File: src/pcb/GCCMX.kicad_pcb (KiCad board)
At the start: 2 copper layers, 341.2 x 155.5 mm, 45 parts, among them J1 Inputs Female, J2 Debug In, J3 Debug Out, J6 USB-IN, J7 USB-OUT, J8 Brook Out

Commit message: pushing everything up from prior work
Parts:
- removed the G*** at (82.0, 207.7) (x2)
- removed the G*** at (228.6, 90.2)
- removed Home, Select: SW_SPST, keyswitches:Kailh_socket_MX+PG1350
- removed J3: Debug Out, Connector_PinHeader_2.54mm:PinHeader_1x07_P2.54mm_Vertical
- removed J6: USB-IN, Connector_PinSocket_2.54mm:PinSocket_1x04_P2.54mm_Vertical
- removed J7: USB-OUT, Connector_PinSocket_2.54mm:PinSocket_1x04_P2.54mm_Vertical
- removed J8: Brook Out, Connector_PinSocket_2.54mm:PinSocket_2x10_P2.54mm_Vertical
- removed the REF** at (276.6, 150.2)
- added D1: 1N5817, Diode_THT:D_DO-41_SOD81_P10.16mm_Horizontal, F.Cu at (224.9, 146.7)
- added G***: LOGO, PriloSilkscreen:PriloSilkscreen, B.Cu at (85.7, 206.4)
- added U1: Pico, RaspberryPiPicoUSB:RPi_Pico_Removed3Pins, F.Cu at (194.9, 193.8)
- J1: value Inputs Female -> Conn_01x04; footprint Connector_PinSocket_2.54mm:PinSocket_2x23_P2.54mm_Vertical -> Model_S:PinHeader_1x04_P2.54mm_Vertical
- J2: value Debug In -> Conn_01x04; footprint Connector_PinSocket_2.54mm:PinSocket_1x06_P2.54mm_Vertical -> Model_S:PinHeader_1x04_P2.54mm_Vertical
- moved J2 65.8 mm to (242.6, 134.6), turned to 180 degrees
- moved J1 64.1 mm to (257.9, 134.6), turned to 180 degrees
- renumbered L to SW1, C-Down to SW10, C-Left to SW11, A to SW12, C-Up to SW13, C-Right to SW14, Up to SW15, Z to SW16, X to SW17, B to SW18, MS to SW19, Left to SW2, LS to SW20, Y to SW21, R to SW22, Down to SW3, Right to SW4, ModX to SW5, ModY to SW6, Start to SW8
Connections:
- J1 pad 1: /TXLED -> Net-(J1-Pad1)
- J1 pad 2: GND -> unconnected-(J1-Pad2)
- J1 pad 3: /L -> /D-
- J1 pad 4: GND -> /D+
- J2 pad 1: Net-(J2-Pad1) -> GND
- J2 pad 3: Net-(J2-Pad3) -> unconnected-(J2-Pad3)
- J2 pad 4: Net-(J2-Pad4) -> /5V
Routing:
- net VBUS: track 173.6 -> 0.00 mm
- net /Right: track 222.8 -> 86.3 mm, vias 4 -> 0
- net GND: track 387.1 -> 253.8 mm, vias 186 -> 174
- net /Down: track 249.6 -> 121.1 mm, vias 5 -> 0
- net /Up: track 323.2 -> 199.0 mm, vias 2 -> 0
- net /Left: track 271.2 -> 148.9 mm, vias 5 -> 0
- net /ModX: track 193.4 -> 71.7 mm, vias 4 -> 0
- net /X: track 278.8 -> 159.5 mm, vias 2 -> 0
- net /Home: track 118.2 -> 0.00 mm, vias 2 -> 0
- net Net-(J6-Pad3): track 104.3 -> 0.00 mm
- net /Z: track 282.9 -> 180.6 mm, vias 2 -> 0
- net Net-(J6-Pad2): track 100.7 -> 0.00 mm
- net /Select: track 97.0 -> 0.00 mm, vias 2 -> 0
- net /B: track 202.8 -> 110.2 mm, vias 2 -> 1
- net /LS: track 270.5 -> 185.7 mm, vias 2 -> 1
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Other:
- net class Default removed
- rule pad_to_mask_clearance: 0.051 -> 0
- board text added: "3V"
- board text added: "5V"
- board text added: "D+"
- board text added: "D-"
- board text added: "D3V"
- board text added: "GND"
- board text added: "Portland Smash"
- board text added: "RX"
- board text added: "TX"
- board text removed: "GCCMX MX Choc Hotswap v1.1"
- board text removed: "Home"
- board text removed: "Select"

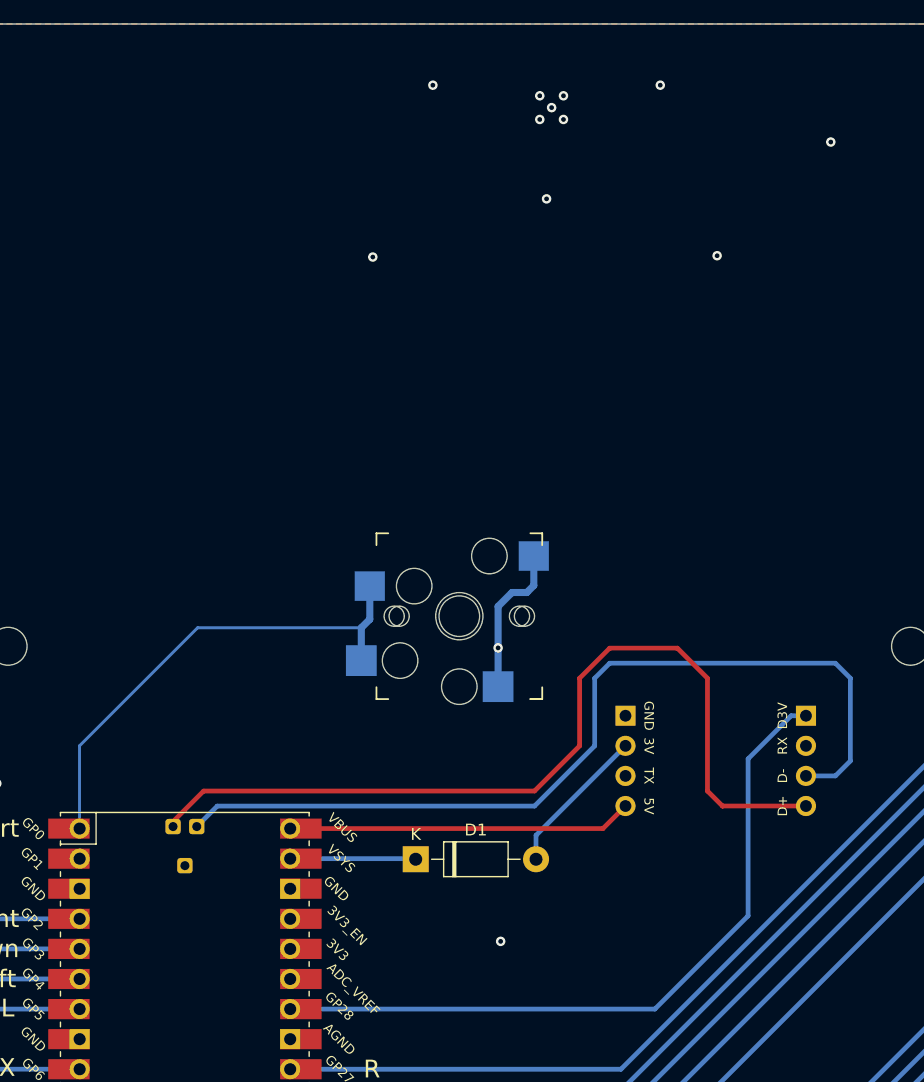
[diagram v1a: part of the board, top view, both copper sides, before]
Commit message: updated pcb, moved USB to front so we no longer require a separate passthrough cable
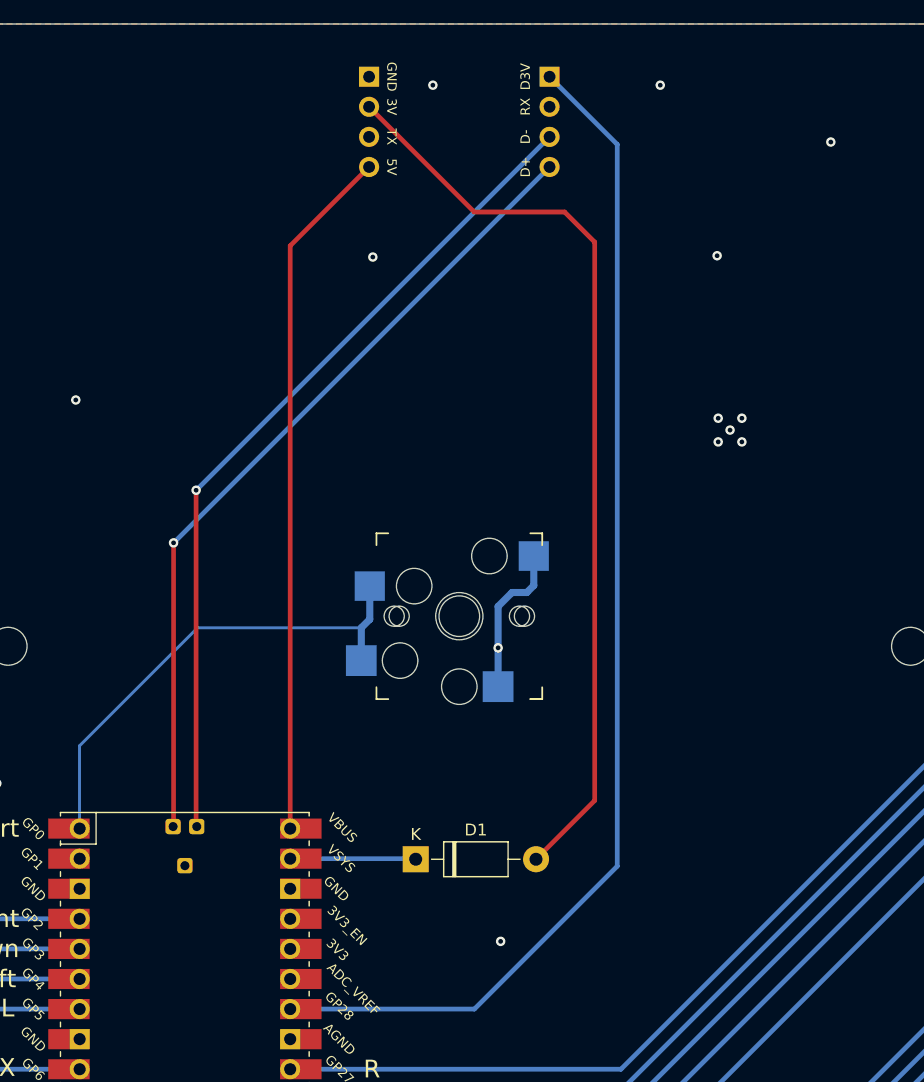
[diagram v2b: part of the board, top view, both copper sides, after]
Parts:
- moved J1 58.1 mm to (236.2, 80.7)
- moved J2 58.1 mm to (221.0, 80.7)
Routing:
- net Net-(D1-Pad2): track 12.7 -> 77.9 mm
- net Net-(J1-Pad1): track 61.6 -> 101.6 mm
- net /5V: track 29.1 -> 58.6 mm
- net /D+: track 74.4 -> 68.9 mm, vias 0 -> 1
- net /D-: track 76.0 -> 70.6 mm, vias 0 -> 1

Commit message: updates
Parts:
- removed D1: 1N5817, Diode_THT:D_DO-41_SOD81_P10.16mm_Horizontal
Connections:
- J2 pad 2: Net-(D1-Pad2) -> unconnected-(J2-Pad2)
- J2 pad 3: unconnected-(J2-Pad3) -> Net-(J2-Pad3)
- U1 pad 39: Net-(D1-Pad1) -> Net-(J2-Pad3)
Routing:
- net Net-(D1-Pad2): track 77.9 -> 0.00 mm
- net Net-(J2-Pad3): track 0.00 -> 75.4 mm
- net Net-(D1-Pad1): track 10.6 -> 0.00 mm

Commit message: looots of case updates. just need to flip the model UD from the back to the front and im ready to test v3 i think
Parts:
- moved J1 9.98 mm to (236.2, 70.7)
- moved J2 9.98 mm to (221.0, 70.7)
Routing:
- net /5V: track 58.6 -> 68.6 mm
- net /D-: track 70.6 -> 80.6 mm
- net /D+: track 68.9 -> 78.8 mm
- net Net-(J1-Pad1): track 101.6 -> 105.9 mm
- net Net-(J2-Pad3): track 75.4 -> 77.8 mm, vias 0 -> 1
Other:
- board size 341.2 x 155.5 mm -> 341.2 x 165.5 mm

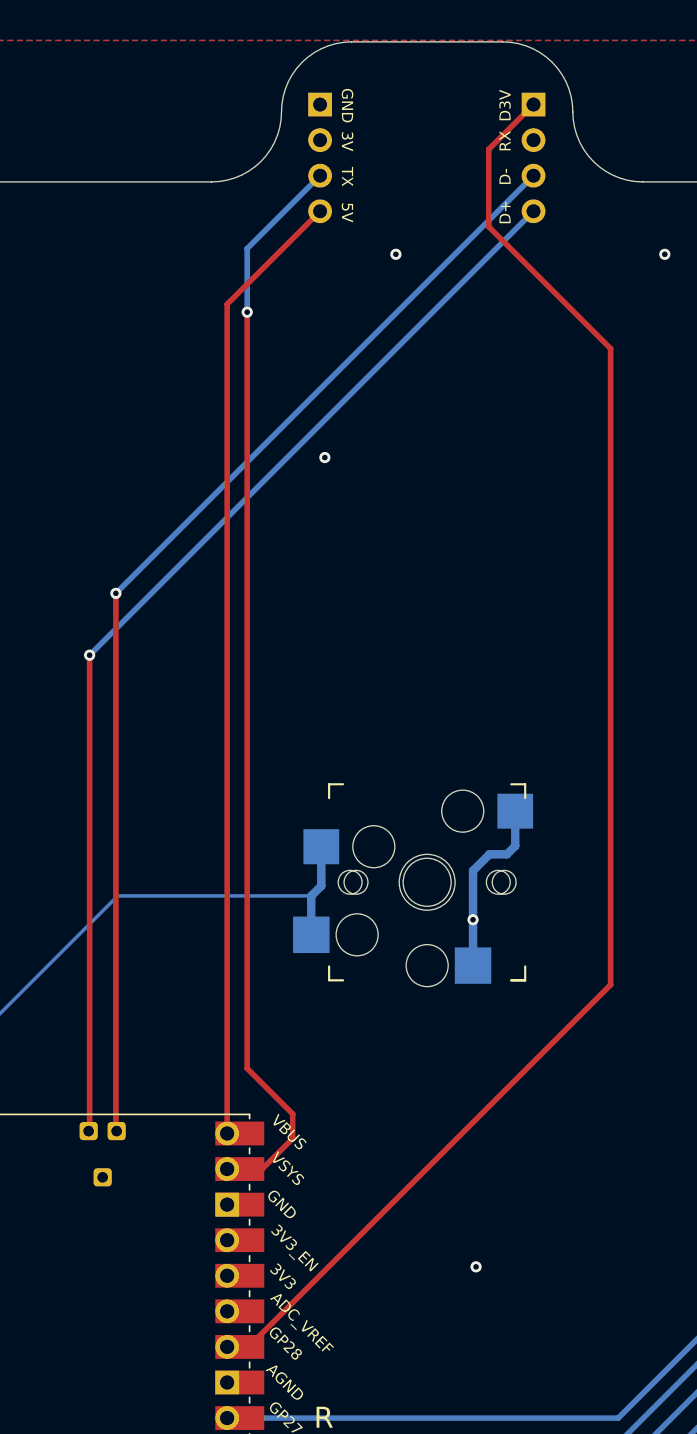
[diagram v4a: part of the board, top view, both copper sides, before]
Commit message: updated PCB to have model UD on top, regenerated fab files
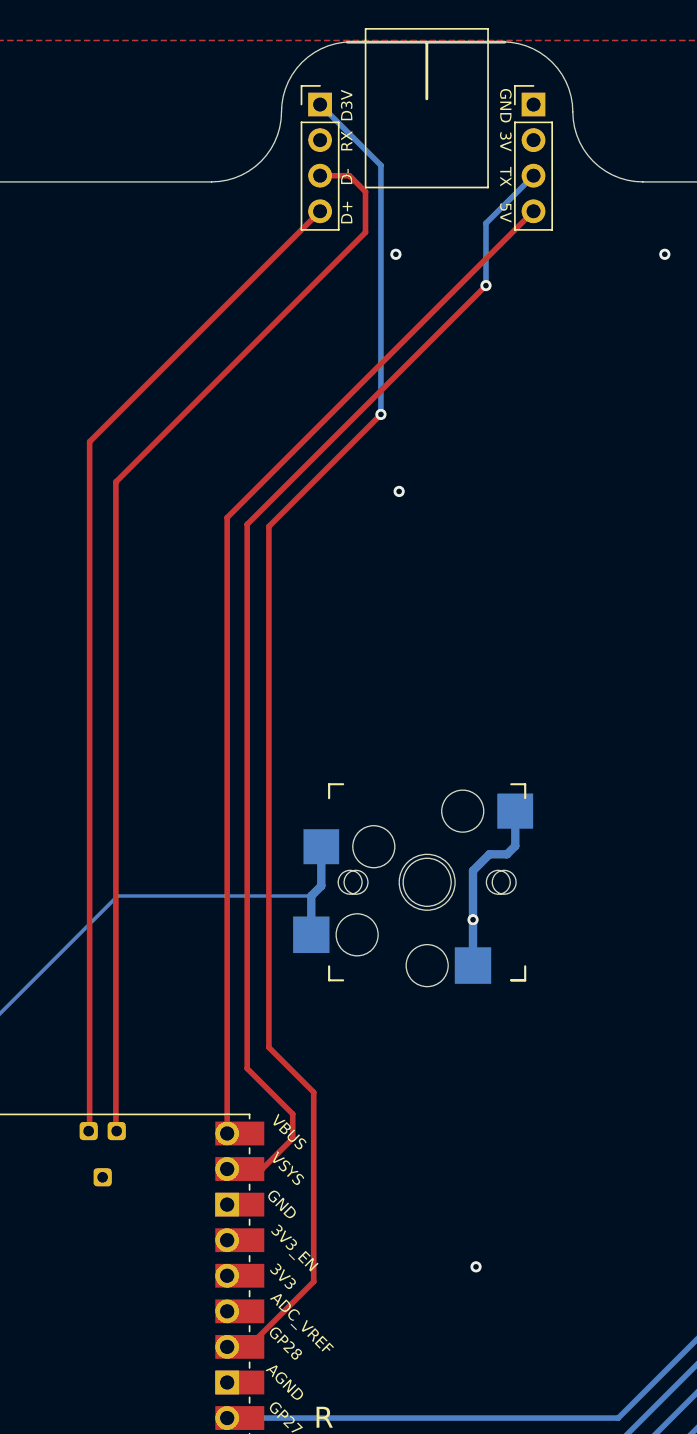
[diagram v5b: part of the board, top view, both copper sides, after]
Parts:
- J1, J2: moved to F.Cu
- moved J1 15.2 mm to (221.0, 70.7), turned to 0 degrees
- moved J2 15.2 mm to (236.2, 70.7), turned to 0 degrees
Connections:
- U1 pad 13: unconnected-(U1-Pad13) -> GND
- U1 pad 18: unconnected-(U1-Pad18) -> GND
- U1 pad 23: unconnected-(U1-Pad23) -> GND
- U1 pad 28: unconnected-(U1-Pad28) -> GND
- U1 pad 3: unconnected-(U1-Pad3) -> GND
- U1 pad 8: unconnected-(U1-Pad8) -> GND
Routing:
- net Net-(J1-Pad1): track 105.9 -> 98.6 mm, vias 0 -> 1
- net /D+: track 78.8 -> 72.5 mm, vias 1 -> 0
- net /5V: track 68.6 -> 74.9 mm
- net Net-(J2-Pad3): track 77.8 -> 84.1 mm
- net /D-: track 80.6 -> 78.2 mm, vias 1 -> 0
